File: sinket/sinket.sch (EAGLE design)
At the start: 4 parts, among them IC1 TINY13-20PU

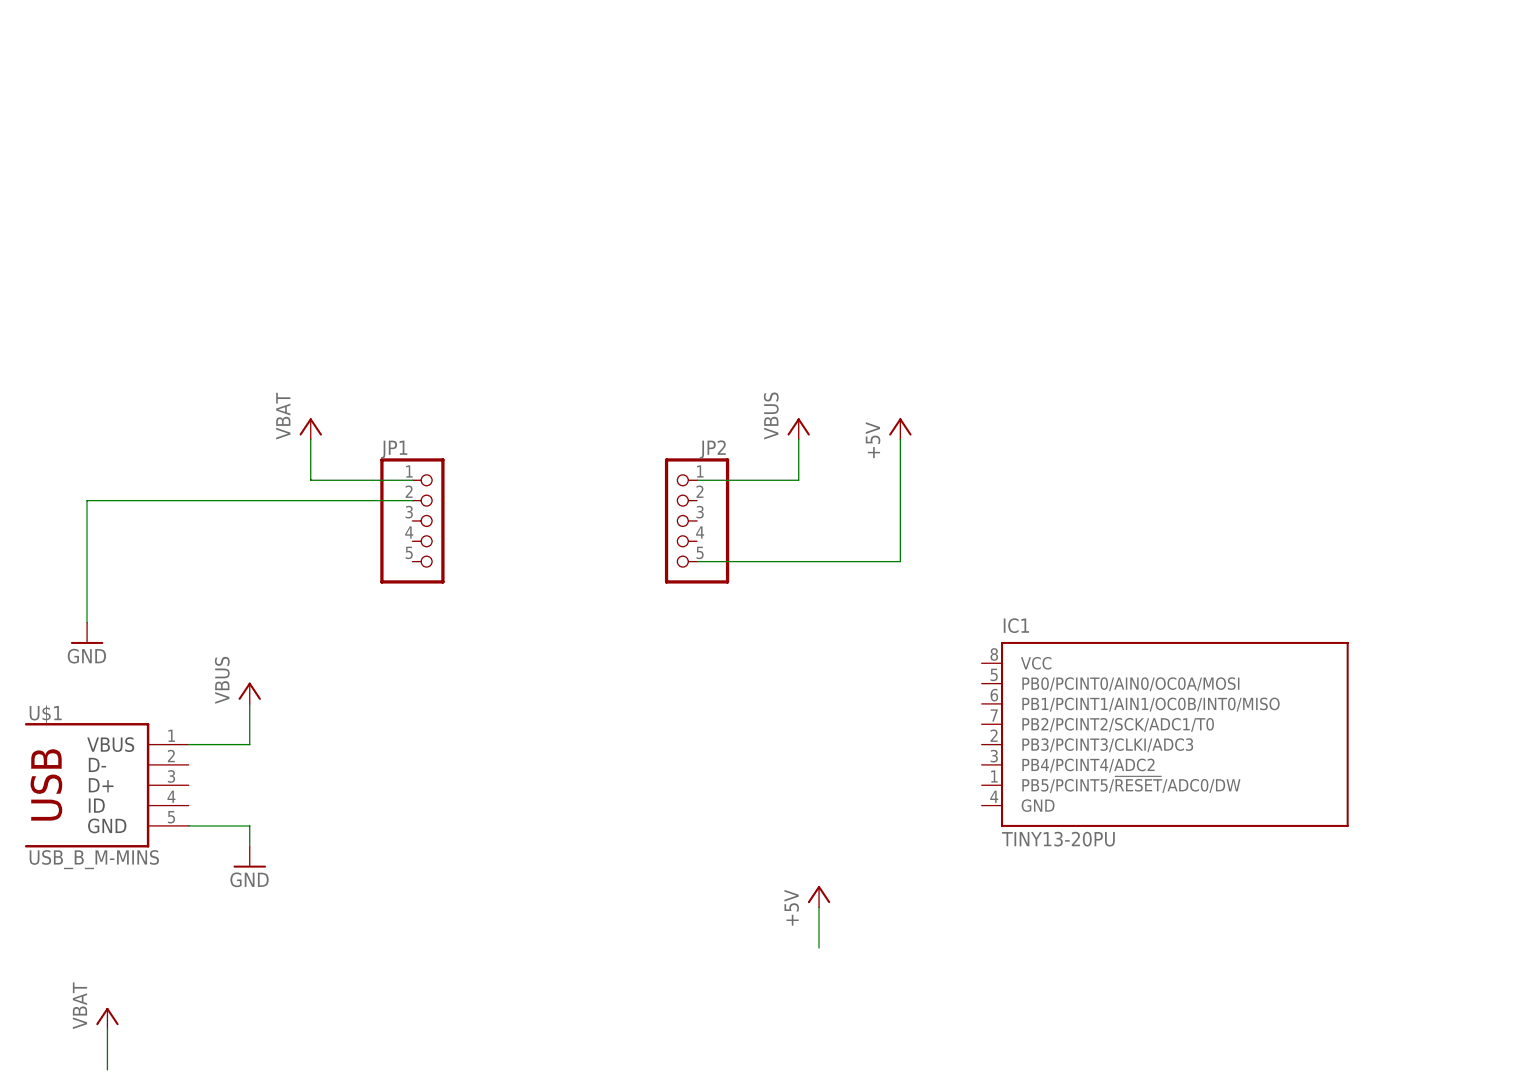
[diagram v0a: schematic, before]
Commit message: replace uC with new ATtiny25 device package symbol
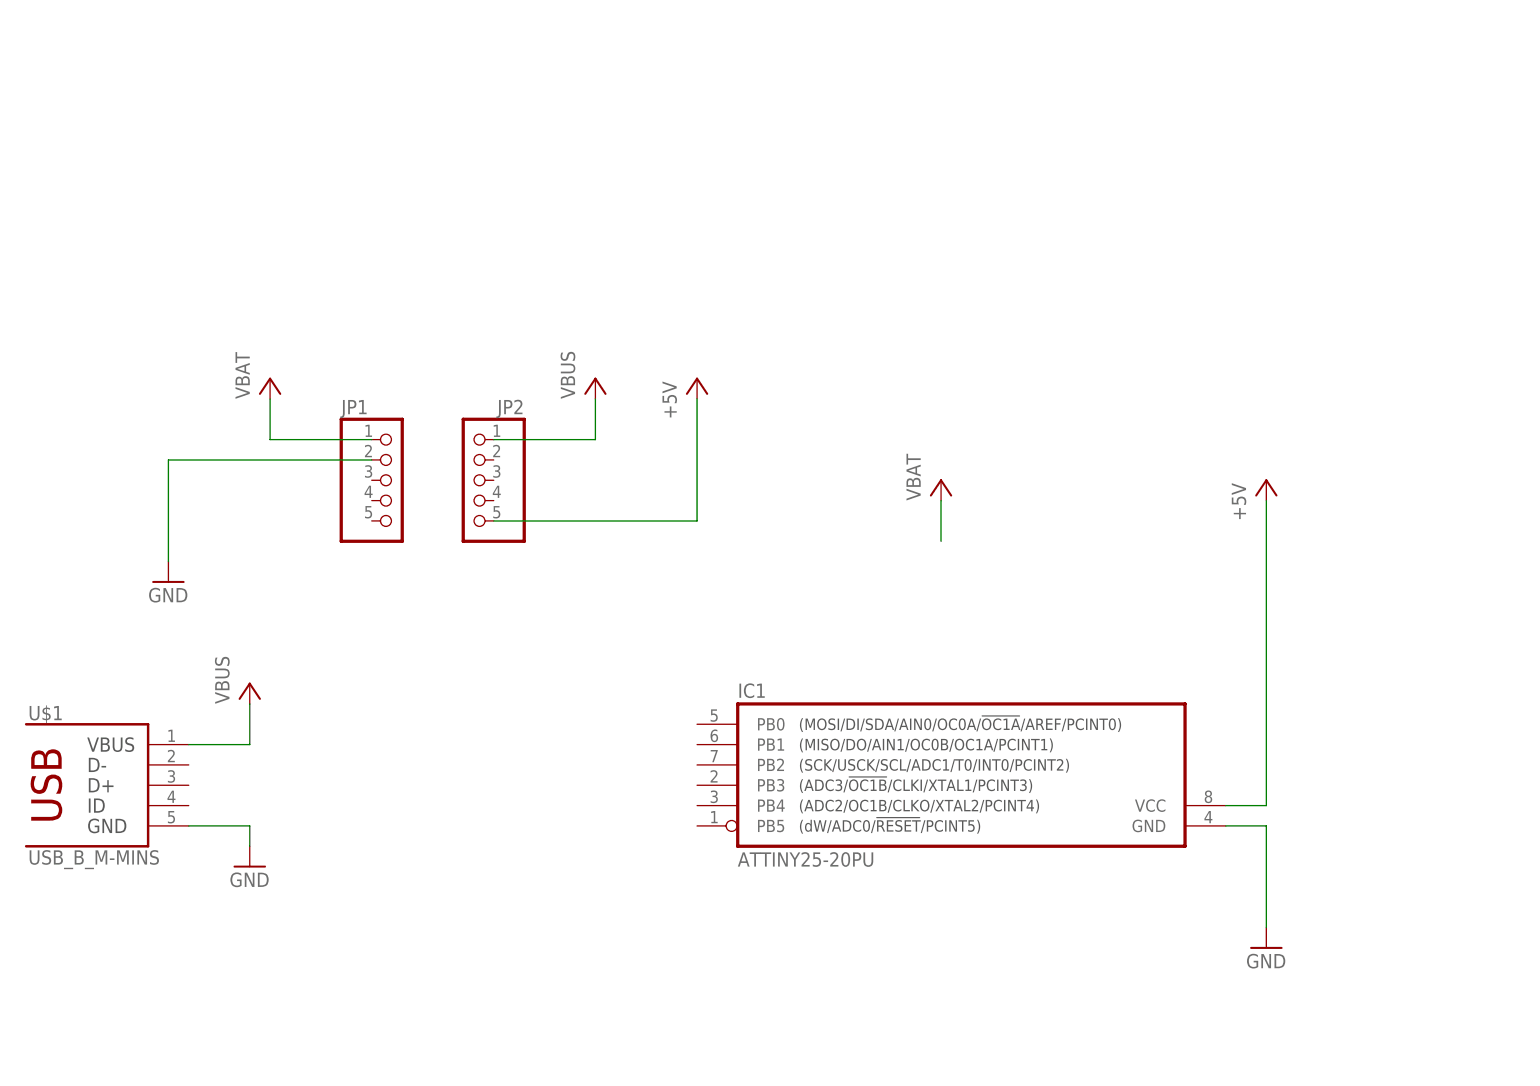
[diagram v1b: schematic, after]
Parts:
- IC1: value TINY13-20PU -> ATTINY25-20PU; device atmel:TINY13-20PU -> n39_avr:ATTINY25-20PU
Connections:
- net +5V: now also IC1.VCC
- net GND: now also IC1.GND
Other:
- moved on the sheet: JP1, JP2
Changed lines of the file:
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@@
 <grid distance="0.1" unitdist="inch" unit="inch" style="lines" multiple="1" display="no" altdistance="0.01" altunitdist="inch" altunit="inch"/>
 <layers>
-<layer number="1" name="Top" color="4" fill="1" visible="yes" active="no"/>
-<layer number="16" name="Bottom" color="1" fill="1" visible="yes" active="no"/>
-<layer number="17" name="Pads" color="2" fill="1" visible="yes" active="no"/>
-<layer number="18" name="Vias" color="2" fill="1" visible="yes" active="no"/>
-<layer number="19" name="Unrouted" color="6" fill="1" visible="yes" active="no"/>
-<layer number="20" name="Dimension" color="15" fill="1" visible="yes" active="no"/>
-<layer number="21" name="tPlace" color="7" fill="1" visible="yes" active="no"/>
-<layer number="22" name="bPlace" color="7" fill="1" visible="yes" active="no"/>
-<layer number="23" name="tOrigins" color="15" fill="1" visible="yes" active="no"/>
-<layer number="24" name="bOrigins" color="15" fill="1" visible="yes" active="no"/>
-<layer number="25" name="tNames" color="7" fill="1" visible="yes" active="no"/>
-<layer number="26" name="bNames" color="7" fill="1" visible="yes" active="no"/>
-<layer number="27" name="tValues" color="7" fill="1" visible="yes" active="no"/>
-<layer number="28" name="bValues" color="7" fill="1" visible="yes" active="no"/>
+<layer number="1" name="Top" color="4" fill="1" visible="no" active="no"/>
+<layer number="16" name="Bottom" color="1" fill="1" visible="no" active="no"/>
+<layer number="17" name="Pads" color="2" fill="1" visible="no" active="no"/>
+<layer number="18" name="Vias" color="2" fill="1" visible="no" active="no"/>
+<layer number="19" name="Unrouted" color="6" fill="1" visible="no" active="no"/>
+<layer number="20" name="Dimension" color="15" fill="1" visible="no" active="no"/>
+<layer number="21" name="tPlace" color="7" fill="1" visible="no" active="no"/>
+<layer number="22" name="bPlace" color="7" fill="1" visible="no" active="no"/>
+<layer number="23" name="tOrigins" color="15" fill="1" visible="no" active="no"/>
+<layer number="24" name="bOrigins" color="15" fill="1" visible="no" active="no"/>
+<layer number="25" name="tNames" color="7" fill="1" visible="no" active="no"/>
+<layer number="26" name="bNames" color="7" fill="1" visible="no" active="no"/>
+<layer number="27" name="tValues" color="7" fill="1" visible="no" active="no"/>
+<layer number="28" name="bValues" color="7" fill="1" visible="no" active="no"/>
 <layer number="29" name="tStop" color="7" fill="3" visible="no" active="no"/>
 <layer number="30" name="bStop" color="7" fill="6" visible="no" active="no"/>
@@
 <layer number="35" name="tGlue" color="7" fill="4" visible="no" active="no"/>
 <layer number="36" name="bGlue" color="7" fill="5" visible="no" active="no"/>
-<layer number="37" name="tTest" color="7" fill="1" visible="yes" active="no"/>
-<layer number="38" name="bTest" color="7" fill="1" visible="yes" active="no"/>
+<layer number="37" name="tTest" color="7" fill="1" visible="no" active="no"/>
+<layer number="38" name="bTest" color="7" fill="1" visible="no" active="no"/>
 <layer number="39" name="tKeepout" color="4" fill="11" visible="no" active="no"/>
 <layer number="40" name="bKeepout" color="1" fill="11" visible="no" active="no"/>
@@
 <layer number="44" name="Drills" color="7" fill="1" visible="no" active="no"/>
 <layer number="45" name="Holes" color="7" fill="1" visible="no" active="no"/>
-<layer number="46" name="Milling" color="3" fill="1" visible="yes" active="no"/>
-<layer number="47" name="Measures" color="7" fill="1" visible="yes" active="no"/>
-<layer number="48" name="Document" color="7" fill="1" visible="yes" active="no"/>
-<layer number="49" name="Reference" color="7" fill="1" visible="yes" active="no"/>
-<layer number="51" name="tDocu" color="7" fill="1" visible="yes" active="no"/>
-<layer number="52" name="bDocu" color="7" fill="1" visible="yes" active="no"/>
+<layer number="46" name="Milling" color="3" fill="1" visible="no" active="no"/>
+<layer number="47" name="Measures" color="7" fill="1" visible="no" active="no"/>
+<layer number="48" name="Document" color="7" fill="1" visible="no" active="no"/>
+<layer number="49" name="Reference" color="7" fill="1" visible="no" active="no"/>
+<layer number="51" name="tDocu" color="7" fill="1" visible="no" active="no"/>
+<layer number="52" name="bDocu" color="7" fill="1" visible="no" active="no"/>
 <layer number="91" name="Nets" color="2" fill="1" visible="yes" active="yes"/>
 <layer number="92" name="Busses" color="1" fill="1" visible="yes" active="yes"/>
@@
 <part name="P+6" library="supply1" deviceset="+5V" device=""/>
 <part name="GND2" library="supply1" deviceset="GND" device=""/>
-<part name="IC1" library="atmel" deviceset="TINY13" device="PU" technology="-20" value="TINY13-20PU"/>
+<part name="IC1" library="n39_avr" deviceset="ATTINY25" device="PU" technology="-20" value="ATTINY25-20PU"/>
+<part name="GND3" library="supply1" deviceset="GND" device=""/>
 </parts>
 <sheets>
@@
 <instance part="P+1" gate="VCC" x="25.4" y="66.04"/>
 <instance part="GND1" gate="1" x="25.4" y="43.18"/>
-<instance part="P+2" gate="VCC" x="7.62" y="25.4"/>
-<instance part="P+3" gate="1" x="96.52" y="40.64"/>
-<instance part="JP1" gate="A" x="48.26" y="86.36"/>
-<instance part="JP2" gate="A" x="78.74" y="86.36" rot="MR0"/>
-<instance part="P+4" gate="VCC" x="93.98" y="99.06"/>
-<instance part="P+5" gate="VCC" x="33.02" y="99.06"/>
-<instance part="P+6" gate="1" x="106.68" y="99.06"/>
-<instance part="GND2" gate="1" x="5.08" y="71.12"/>
-<instance part="IC1" gate="G$1" x="137.16" y="55.88"/>
+<instance part="P+2" gate="VCC" x="111.76" y="91.44"/>
+<instance part="P+3" gate="1" x="152.4" y="91.44"/>
+<instance part="JP1" gate="A" x="43.18" y="91.44"/>
+<instance part="JP2" gate="A" x="53.34" y="91.44" rot="MR0"/>
+<instance part="P+4" gate="VCC" x="68.58" y="104.14"/>
+<instance part="P+5" gate="VCC" x="27.94" y="104.14"/>
+<instance part="P+6" gate="1" x="81.28" y="104.14"/>
+<instance part="GND2" gate="1" x="15.24" y="78.74"/>
+<instance part="IC1" gate="G$1" x="111.76" y="55.88"/>
+<instance part="GND3" gate="1" x="152.4" y="33.02"/>
 </instances>
 <busses>
 </busses>
 <nets>
-<net name="VBAT" class="0">
+<net name="VBAT" class="1">
 <segment>
 <pinref part="P+2" gate="VCC" pin="VCC"/>
-<wire x1="7.62" y1="22.86" x2="7.62" y2="17.78" width="0.1524" layer="91"/>
+<wire x1="111.76" y1="88.9" x2="111.76" y2="83.82" width="0.1524" layer="91"/>
 </segment>
 <segment>
 <pinref part="JP1" gate="A" pin="1"/>
-<wire x1="45.72" y1="91.44" x2="33.02" y2="91.44" width="0.1524" layer="91"/>
-<wire x1="33.02" y1="91.44" x2="33.02" y2="96.52" width="0.1524" layer="91"/>
+<wire x1="40.64" y1="96.52" x2="27.94" y2="96.52" width="0.1524" layer="91"/>
+<wire x1="27.94" y1="96.52" x2="27.94" y2="101.6" width="0.1524" layer="91"/>
 <pinref part="P+5" gate="VCC" pin="VCC"/>
 </segment>
 </net>
-<net name="+5V" class="0">
+<net name="+5V" class="1">
 <segment>
 <pinref part="P+3" gate="1" pin="+5V"/>
-<wire x1="96.52" y1="38.1" x2="96.52" y2="33.02" width="0.1524" layer="91"/>
+<wire x1="152.4" y1="88.9" x2="152.4" y2="50.8" width="0.1524" layer="91"/>
+<pinref part="IC1" gate="G$1" pin="VCC"/>
+<wire x1="152.4" y1="50.8" x2="147.32" y2="50.8" width="0.1524" layer="91"/>
 </segment>
 <segment>
 <pinref part="JP2" gate="A" pin="5"/>
-<wire x1="81.28" y1="81.28" x2="106.68" y2="81.28" width="0.1524" layer="91"/>
-<wire x1="106.68" y1="81.28" x2="106.68" y2="96.52" width="0.1524" layer="91"/>
+<wire x1="55.88" y1="86.36" x2="81.28" y2="86.36" width="0.1524" layer="91"/>
+<wire x1="81.28" y1="86.36" x2="81.28" y2="101.6" width="0.1524" layer="91"/>
 <pinref part="P+6" gate="1" pin="+5V"/>
 </segment>
 </net>
-<net name="VBUS" class="0">
+<net name="VBUS" class="1">
 <segment>
 <pinref part="P+1" gate="VCC" pin="VCC"/>
@@
 <segment>
 <pinref part="JP2" gate="A" pin="1"/>
-<wire x1="81.28" y1="91.44" x2="93.98" y2="91.44" width="0.1524" layer="91"/>
-<wire x1="93.98" y1="91.44" x2="93.98" y2="96.52" width="0.1524" layer="91"/>
+<wire x1="55.88" y1="96.52" x2="68.58" y2="96.52" width="0.1524" layer="91"/>
+<wire x1="68.58" y1="96.52" x2="68.58" y2="101.6" width="0.1524" layer="91"/>
 <pinref part="P+4" gate="VCC" pin="VCC"/>
 </segment>
 </net>
-<net name="GND" class="0">
+<net name="GND" class="1">
 <segment>
 <pinref part="U$1" gate="G$1" pin="5"/>
@@
 <segment>
 <pinref part="JP1" gate="A" pin="2"/>
-<wire x1="45.72" y1="88.9" x2="5.08" y2="88.9" width="0.1524" layer="91"/>
-<wire x1="5.08" y1="88.9" x2="5.08" y2="73.66" width="0.1524" layer="91"/>
+<wire x1="40.64" y1="93.98" x2="15.24" y2="93.98" width="0.1524" layer="91"/>
+<wire x1="15.24" y1="93.98" x2="15.24" y2="81.28" width="0.1524" layer="91"/>
 <pinref part="GND2" gate="1" pin="GND"/>
 </segment>
+<segment>
+<pinref part="IC1" gate="G$1" pin="GND"/>
+<wire x1="147.32" y1="48.26" x2="152.4" y2="48.26" width="0.1524" layer="91"/>
+<wire x1="152.4" y1="48.26" x2="152.4" y2="35.56" width="0.1524" layer="91"/>
+<pinref part="GND3" gate="1" pin="GND"/>
+</segment>
 </net>

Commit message: proceed schematics (stopped because a schottky diode is missing)
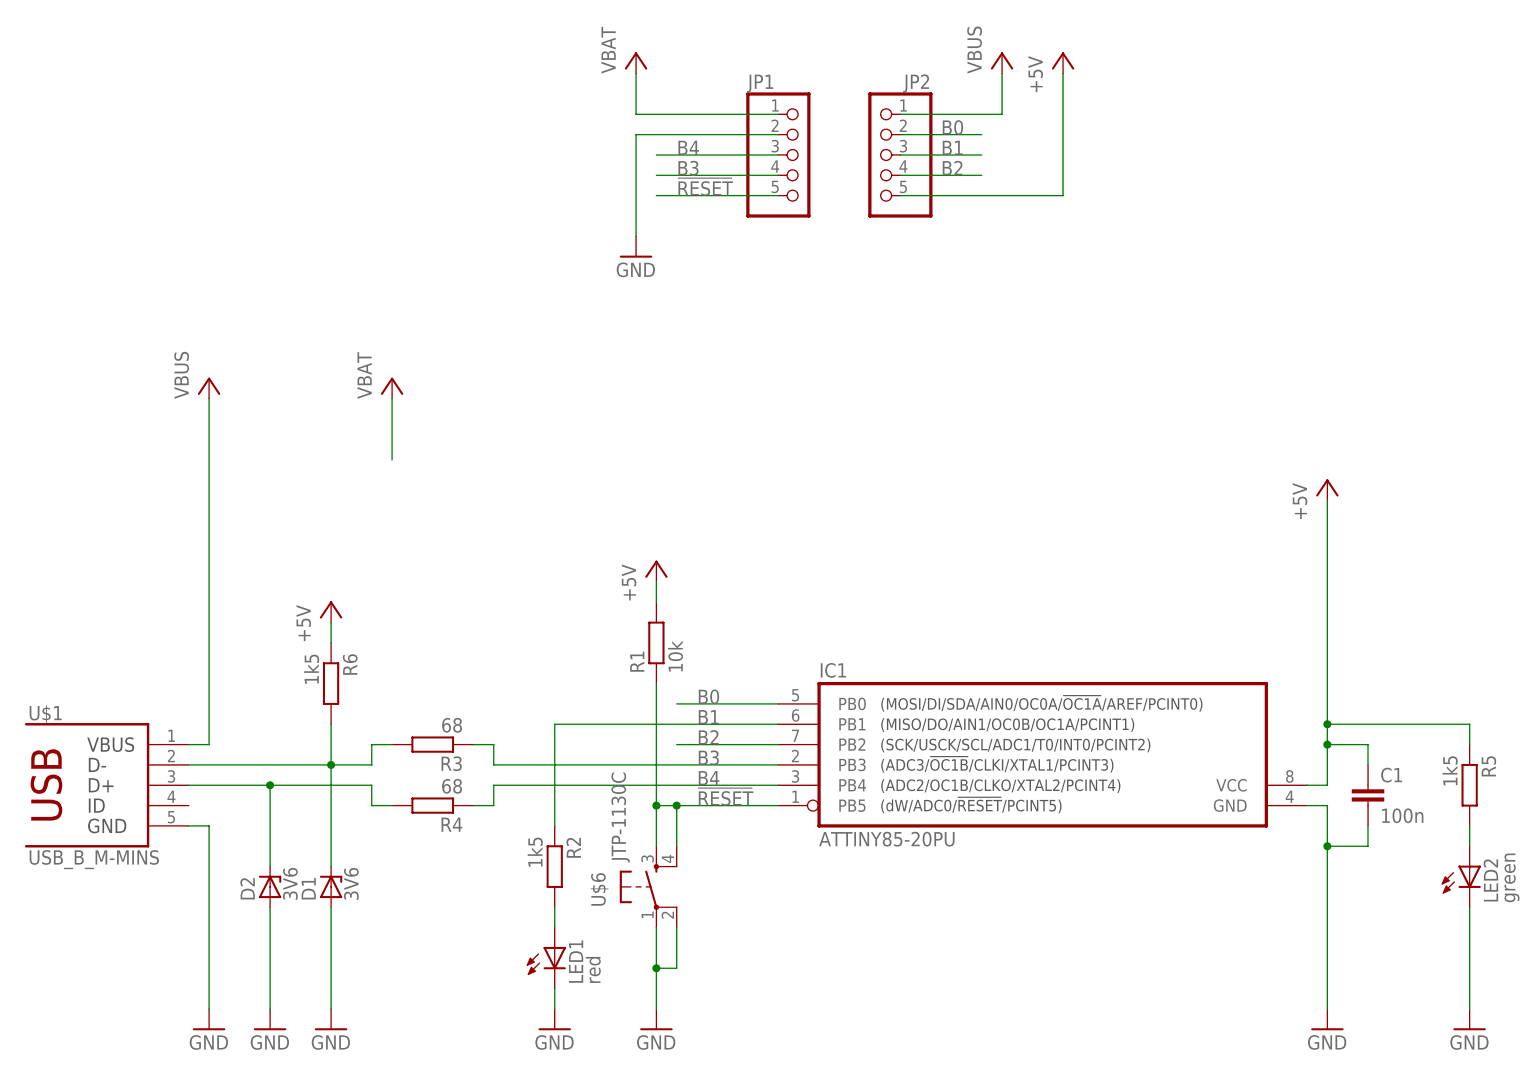
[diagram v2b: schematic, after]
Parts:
- added C1: 100n, rcl:C-EUC0805
- added D1, D2: 3V6, diode:ZENER-DIODESOD80C
- added LED1: red, led:LED3MM
- added LED2: green, led:LED3MM
- added R1: 10k, rcl:R-EU_R0805
- added R2, R5, R6: 1k5, rcl:R-EU_R0805
- added R3, R4: 68, rcl:R-EU_R0805
- added U$6: JTP-1130C, n39:JTP-1130C
- IC1: value ATTINY25-20PU -> ATTINY85-20PU
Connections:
- new net !RESET: IC1.PB5, JP1.5, R1.1, U$6.S, U$6.S1
- new net B0: IC1.PB0, JP2.2
- new net B1: IC1.PB1, JP2.3, R2.1
- new net B2: IC1.PB2, JP2.4
- new net B3: IC1.PB3, JP1.4, R3.1
- new net B4: IC1.PB4, JP1.3, R4.1
- new net N$1: D1.C, R3.2, R6.2, U$1.2
- new net N$3: D2.C, R4.2, U$1.3
- new net N$4: LED1.A, R2.2
- new net N$5: LED2.A, R5.2
- net +5V: now also C1.1, R1.2, R5.1, R6.1
- net GND: now also C1.2, D1.A, D2.A, LED1.C, LED2.C, U$6.P, U$6.P1
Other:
- moved on the sheet: IC1, JP1, JP2
